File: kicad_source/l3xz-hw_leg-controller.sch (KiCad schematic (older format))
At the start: 36 parts, among them CN1 ARDUINO_NANO_33, CN2 SM04B-SRSS-TB, CN3 SM04B-SRSS-TB, CN6 691322310002, CN7 CONN_02X03, CN8 691382010002, U3 24LC64

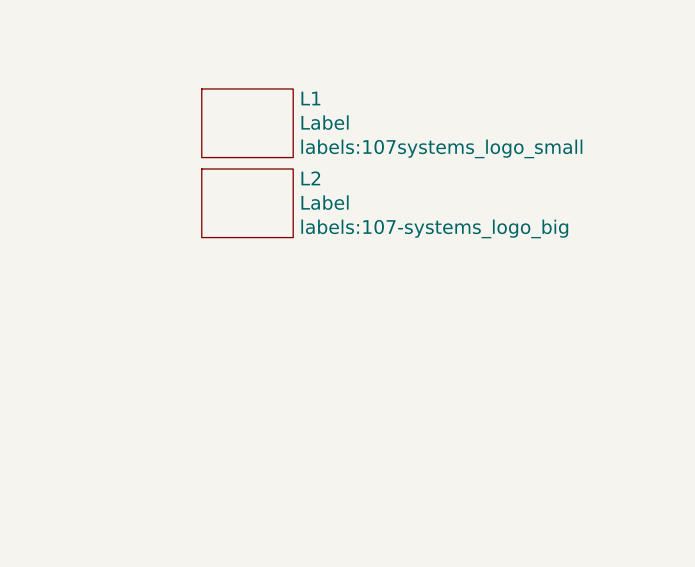
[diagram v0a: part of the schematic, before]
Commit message: added alternative DIL package for MCP2515
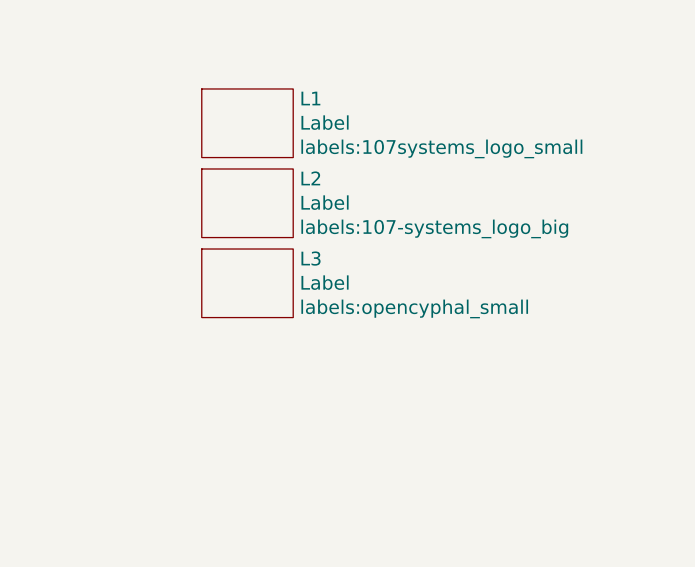
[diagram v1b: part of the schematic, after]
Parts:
- added L3: Label, labels:opencyphal_small, symbol devices:Label
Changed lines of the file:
@@
 Sheet 1 3
 Title "l3xz-hw_leg-controller"
-Date "2022-04-10"
+Date "2022-04-12"
 Rev "0.1"
 Comp "107-systems"
@@
 	1    0    0    -1
 $EndComp
+$Comp
+L devices:Label L3
+U 1 1 625E2D3C
+P 9450 5950
+F 0 "L3" H 9678 6056 60  0000 L CNN
+F 1 "Label" H 9678 5950 60  0000 L CNN
+F 2 "labels:opencyphal_small" H 9678 5844 60  0000 L CNN
+F 3 "" H 9450 5950 60  0000 C CNN
+	1    9450 5950
+	1    0    0    -1
+$EndComp

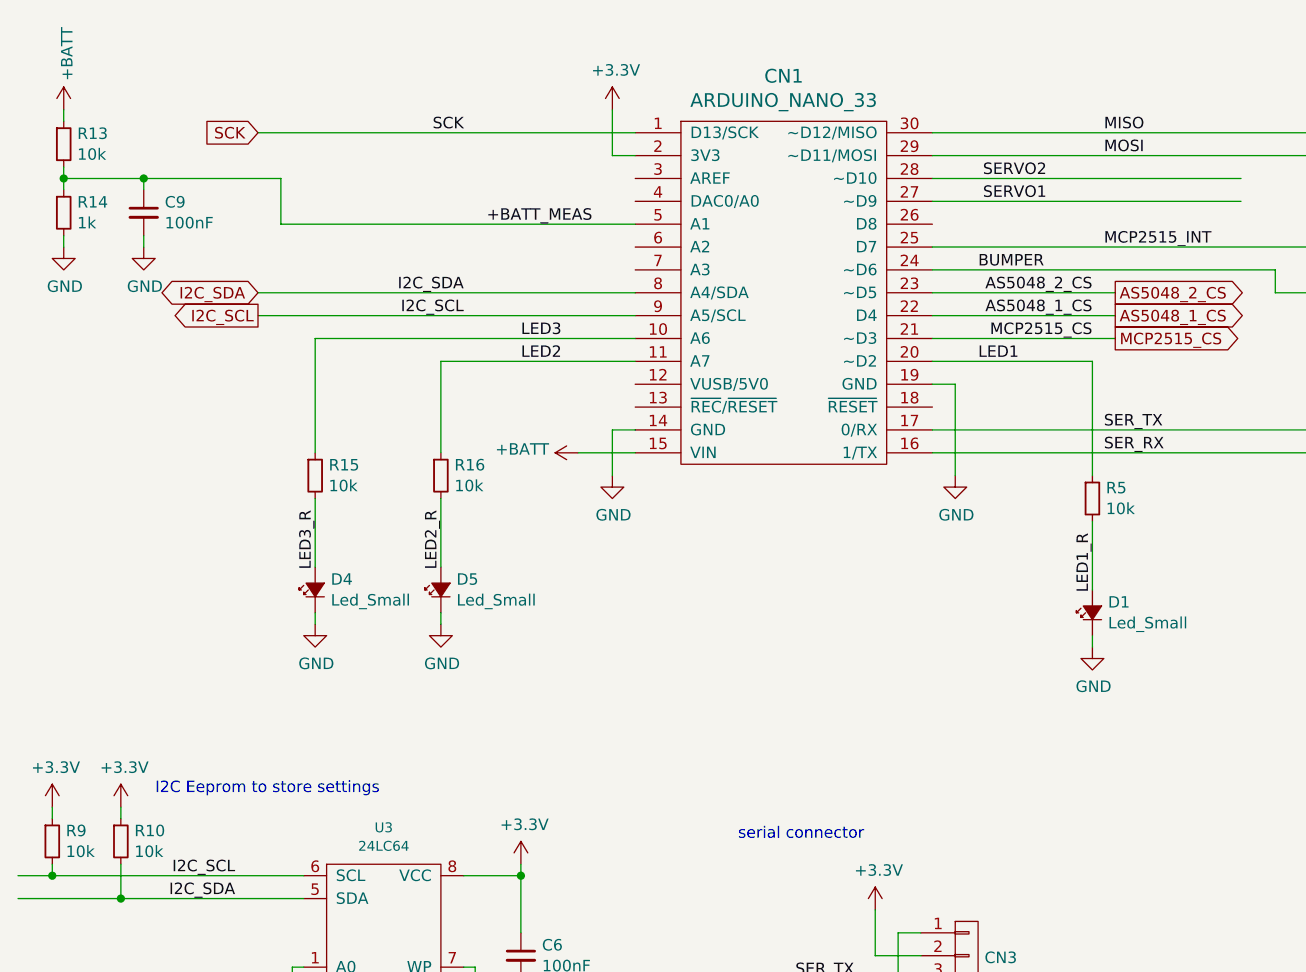
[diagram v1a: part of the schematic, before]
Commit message: updated some part values
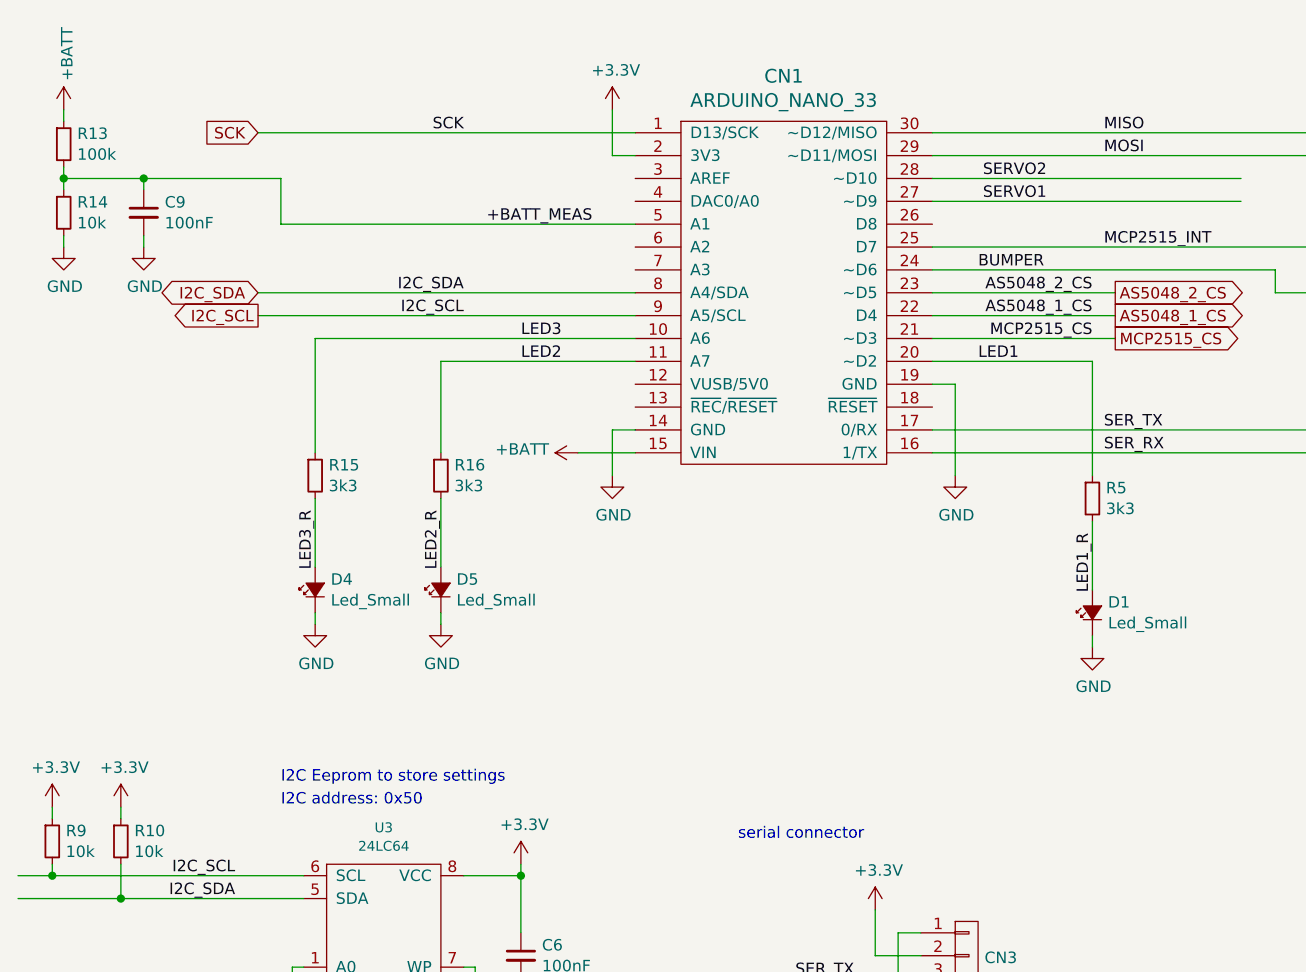
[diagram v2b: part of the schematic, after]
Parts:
- R13: value 10k -> 100k
- R14: value 1k -> 10k
- R15, R16, R5: value 10k -> 3k3
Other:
- note added: "I2C address: 0x50"
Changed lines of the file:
@@
 AR Path="/624BFD41" Ref="R5"  Part="1"
 F 0 "R5" H 5409 2996 50  0000 L CNN
-F 1 "10k" H 5409 2905 50  0000 L CNN
+F 1 "3k3" H 5409 2905 50  0000 L CNN
 F 2 "resistors:R_0603" H 5350 2800 50  0001 C CNN
 F 3 "" H 5350 2950 50  0000 C CNN
@@
 Text Label 1600 4600 2    50   ~ 0
 I2C_SCL
-Text Notes 1250 4250 0    50   ~ 0
+Text Notes 1800 4200 0    50   ~ 0
 I2C Eeprom to store settings
 $Comp
@@
 AR Path="/6256C3A2" Ref="R16"  Part="1"
 F 0 "R16" H 2559 2896 50  0000 L CNN
-F 1 "10k" H 2559 2805 50  0000 L CNN
+F 1 "3k3" H 2559 2805 50  0000 L CNN
 F 2 "resistors:R_0603" H 2500 2700 50  0001 C CNN
 F 3 "" H 2500 2850 50  0000 C CNN
@@
 AR Path="/625730AD" Ref="R15"  Part="1"
 F 0 "R15" H 2009 2896 50  0000 L CNN
-F 1 "10k" H 2009 2805 50  0000 L CNN
+F 1 "3k3" H 2009 2805 50  0000 L CNN
 F 2 "resistors:R_0603" H 1950 2700 50  0001 C CNN
 F 3 "" H 1950 2850 50  0000 C CNN
@@
 AR Path="/62580A99" Ref="R13"  Part="1"
 F 0 "R13" H 909 1446 50  0000 L CNN
-F 1 "10k" H 909 1355 50  0000 L CNN
+F 1 "100k" H 909 1355 50  0000 L CNN
 F 2 "resistors:R_0603" H 850 1250 50  0001 C CNN
 F 3 "" H 850 1400 50  0000 C CNN
@@
 AR Path="/62580F1D" Ref="R14"  Part="1"
 F 0 "R14" H 909 1746 50  0000 L CNN
-F 1 "1k" H 909 1655 50  0000 L CNN
+F 1 "10k" H 909 1655 50  0000 L CNN
 F 2 "resistors:R_0603" H 850 1550 50  0001 C CNN
 F 3 "" H 850 1700 50  0000 C CNN
@@
 	1    0    0    -1
 $EndComp
+Text Notes 1800 4300 0    50   ~ 0
+I2C address: 0x50
 $EndSCHEMATC

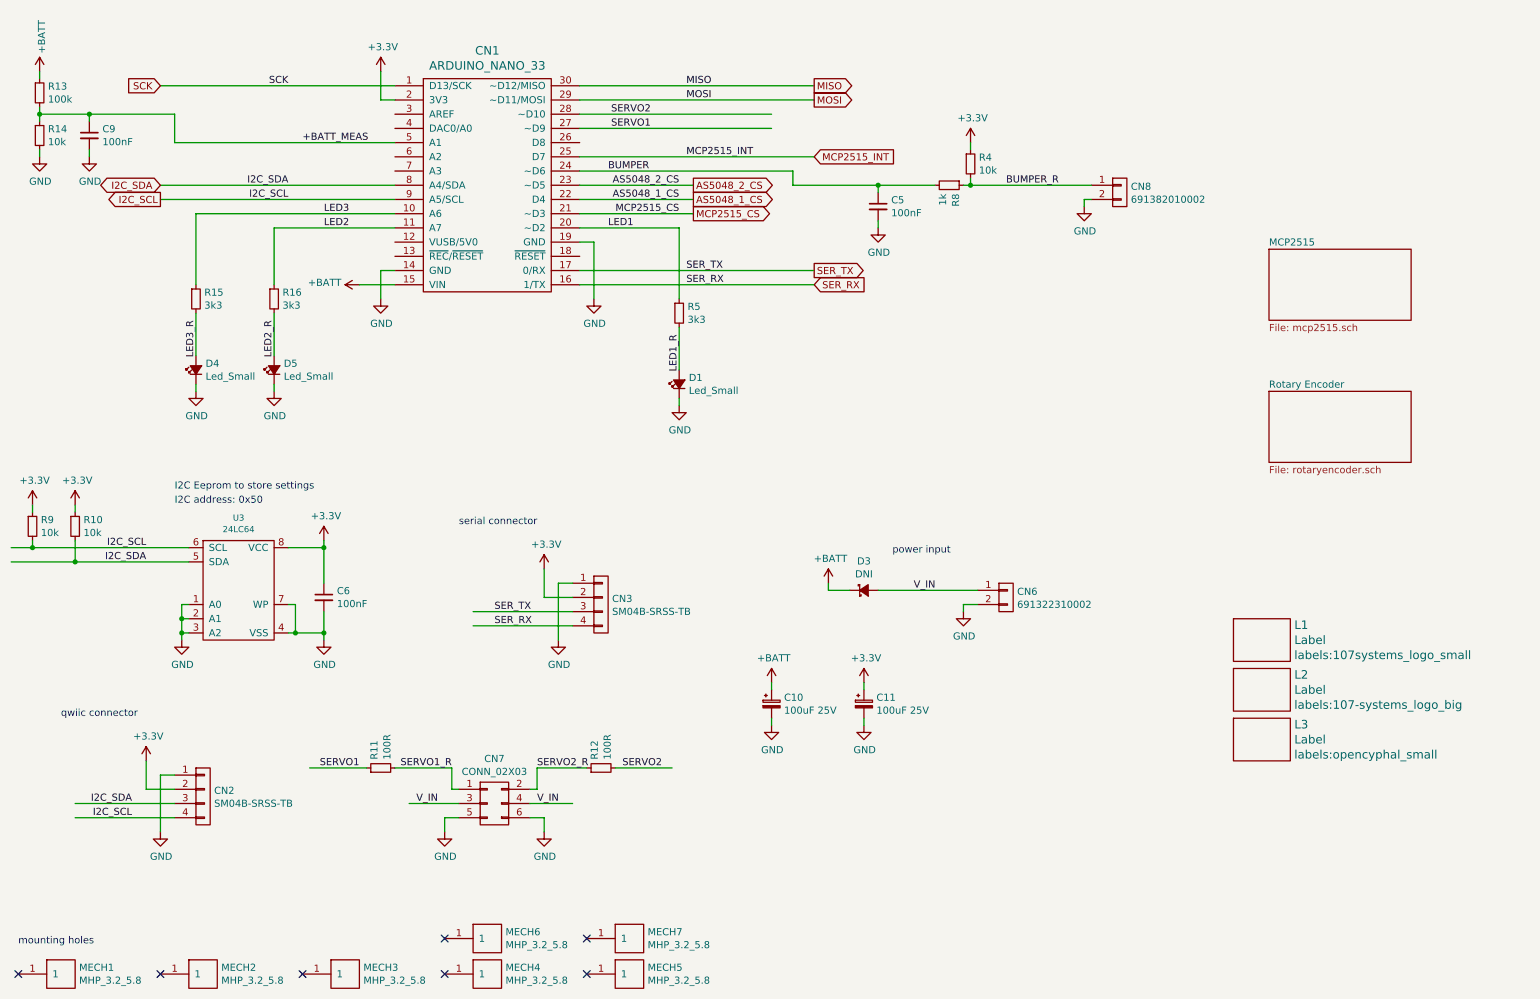
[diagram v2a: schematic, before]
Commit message: updated BOM in readme and schematic, updated schematic pdf
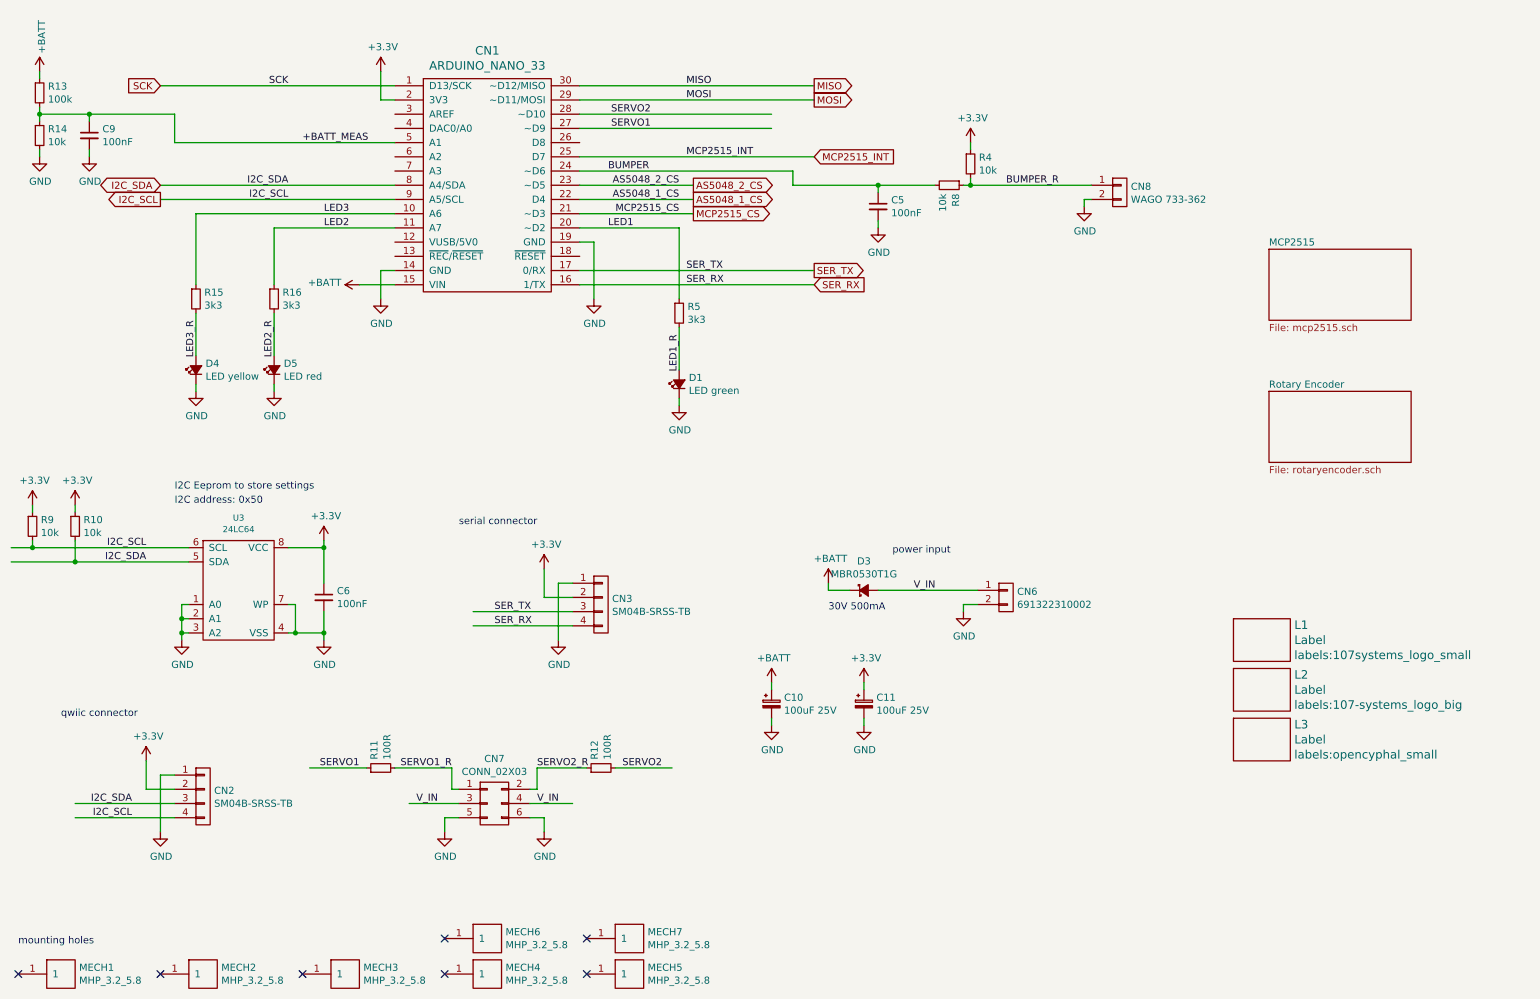
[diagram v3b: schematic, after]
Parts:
- CN8: value 691382010002 -> WAGO 733-362
- D1: value Led_Small -> LED green
- D3: value DNI -> MBR0530T1G
- D4: value Led_Small -> LED yellow
- D5: value Led_Small -> LED red
- R8: value 1k -> 10k
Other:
- note added: "30V 500mA"
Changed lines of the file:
@@
 Sheet 1 3
 Title "l3xz-hw_leg-controller"
-Date "2022-04-12"
+Date "2022-05-29"
 Rev "0.1"
 Comp "107-systems"
@@
 P 5350 3450
 F 0 "D1" V 5396 3382 50  0000 R CNN
-F 1 "Led_Small" V 5305 3382 50  0000 R CNN
+F 1 "LED green" V 5305 3382 50  0000 R CNN
 F 2 "LEDs:LED_0603" V 5350 3450 50  0001 C CNN
 F 3 "" V 5350 3450 50  0000 C CNN
@@
 P 8450 2100
 F 0 "CN8" H 8528 2141 50  0000 L CNN
-F 1 "691382010002" H 8528 2050 50  0000 L CNN
+F 1 "WAGO 733-362" H 8528 2050 50  0000 L CNN
 F 2 "CON_wuerth:WR-TBL_691382010002" H 8528 2004 50  0001 L CNN
 F 3 "" H 8450 2100 50  0000 C CNN
@@
 AR Path="/62508153" Ref="R8"  Part="1"
 F 0 "R8" H 7309 2096 50  0000 L CNN
-F 1 "1k" H 7309 2005 50  0000 L CNN
+F 1 "10k" H 7309 2005 50  0000 L CNN
 F 2 "resistors:R_0603" H 7250 1900 50  0001 C CNN
 F 3 "" H 7250 2050 50  0000 C CNN
@@
 AR Path="/62533088" Ref="D3"  Part="1"
 F 0 "D3" H 6650 5105 50  0000 C CNN
-F 1 "DNI" H 6650 5014 50  0000 C CNN
+F 1 "MBR0530T1G" H 6650 5014 50  0000 C CNN
 F 2 "diodes:SOD-123" V 6650 4900 50  0001 C CNN
 F 3 "" V 6650 4900 50  0000 C CNN
@@
 P 2500 3350
 F 0 "D5" V 2546 3282 50  0000 R CNN
-F 1 "Led_Small" V 2455 3282 50  0000 R CNN
+F 1 "LED red" V 2455 3282 50  0000 R CNN
 F 2 "LEDs:LED_0603" V 2500 3350 50  0001 C CNN
 F 3 "" V 2500 3350 50  0000 C CNN
@@
 P 1950 3350
 F 0 "D4" V 1996 3282 50  0000 R CNN
-F 1 "Led_Small" V 1905 3282 50  0000 R CNN
+F 1 "LED yellow" V 1905 3282 50  0000 R CNN
 F 2 "LEDs:LED_0603" V 1950 3350 50  0001 C CNN
 F 3 "" V 1950 3350 50  0000 C CNN
@@
 Text Notes 1800 4300 0    50   ~ 0
 I2C address: 0x50
+Text Notes 6400 5050 0    50   ~ 0
+30V 500mA
 $EndSCHEMATC

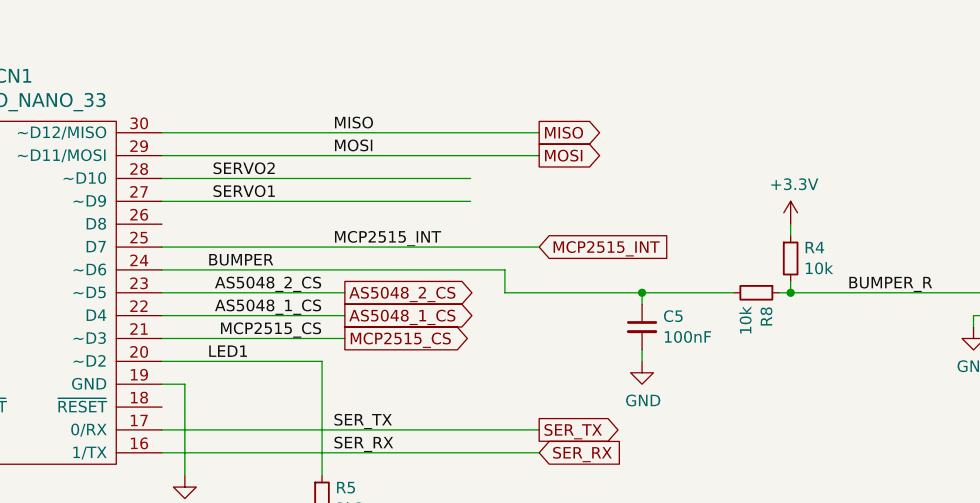
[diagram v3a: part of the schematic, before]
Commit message: exchanged pin D7 and D9 and connected U9, pin8 to GND in readme and schematic as all boards have been reworked
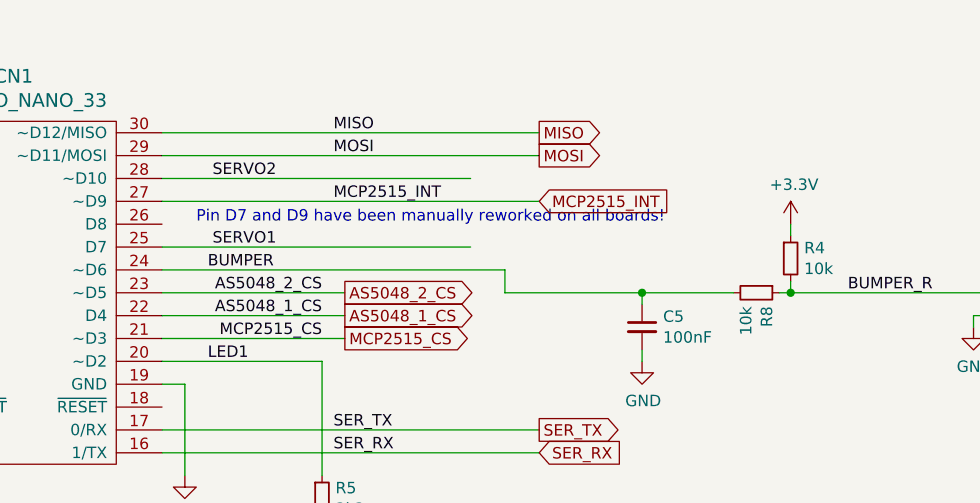
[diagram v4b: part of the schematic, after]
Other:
- note added: "Pin D7 and D9 have been manually reworked on all boards!"
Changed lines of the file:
@@
 SER_TX
 Wire Wire Line
-	6300 1850 4650 1850
+	6300 1650 4650 1650
 Wire Wire Line
 	6300 1450 4650 1450
-Text Label 5400 1850 0    50   ~ 0
+Text Label 5400 1650 0    50   ~ 0
 MCP2515_INT
 Text Label 5400 1450 0    50   ~ 0
 MOSI
-Text GLabel 6300 1850 2    50   Input ~ 0
+Text GLabel 6300 1650 2    50   Input ~ 0
 MCP2515_INT
 Text GLabel 6300 1450 2    50   Output ~ 0
@@
 SERVO2
 Wire Wire Line
-	6000 1650 4650 1650
+	6000 1850 4650 1850
 Wire Wire Line
 	4650 1550 6000 1550
 Text Label 5150 1550 2    50   ~ 0
 SERVO2
-Text Label 5150 1650 2    50   ~ 0
+Text Label 5150 1850 2    50   ~ 0
 SERVO1
 $Comp
@@
 Text Notes 6400 5050 0    50   ~ 0
 30V 500mA
+Text Notes 4800 1750 0    50   ~ 0
+Pin D7 and D9 have been manually reworked on all boards!
 $EndSCHEMATC

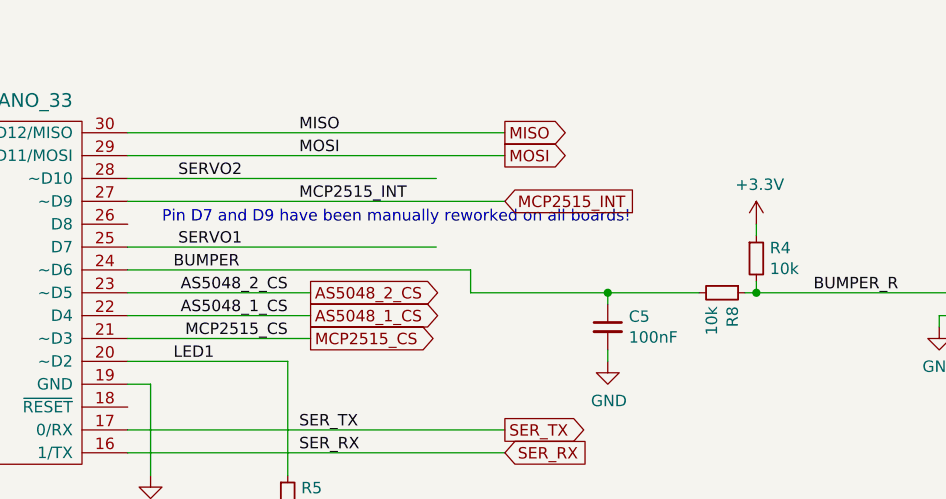
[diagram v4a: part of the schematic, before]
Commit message: fixed MCP2515_INT and direction label for Arduino
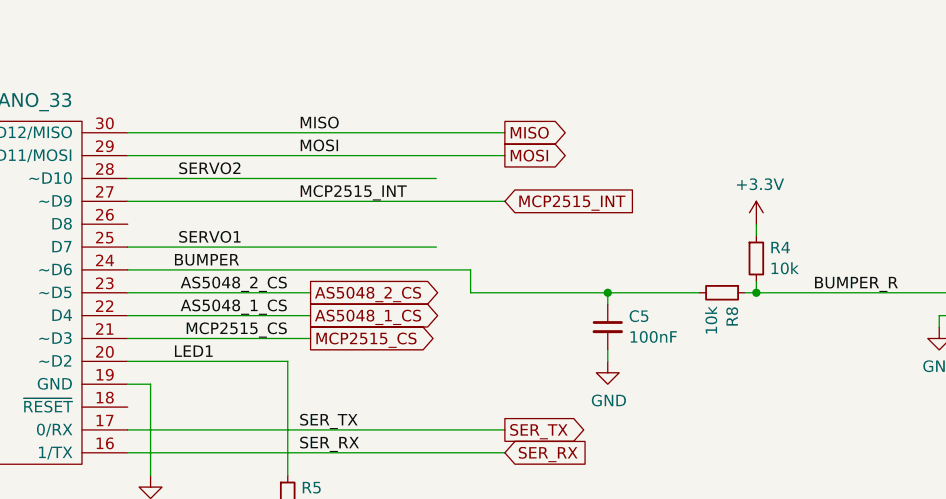
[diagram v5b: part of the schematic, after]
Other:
- note removed: "Pin D7 and D9 have been manually reworked on all boards!"
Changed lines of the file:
@@
 Sheet 1 3
 Title "l3xz-hw_leg-controller"
-Date "2022-05-29"
-Rev "0.1"
+Date "2022-06-05"
+Rev "dev_0.2"
 Comp "107-systems"
 Comment1 ""
@@
 Text Notes 6400 5050 0    50   ~ 0
 30V 500mA
-Text Notes 4800 1750 0    50   ~ 0
-Pin D7 and D9 have been manually reworked on all boards!
 $EndSCHEMATC
